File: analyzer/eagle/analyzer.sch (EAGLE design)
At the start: 32 parts, among them J4 USBSMD, U1 ATA6631, U2 FT232RL, U3 ATMEGA328P, U4 MOCD208M, X1 16MHz

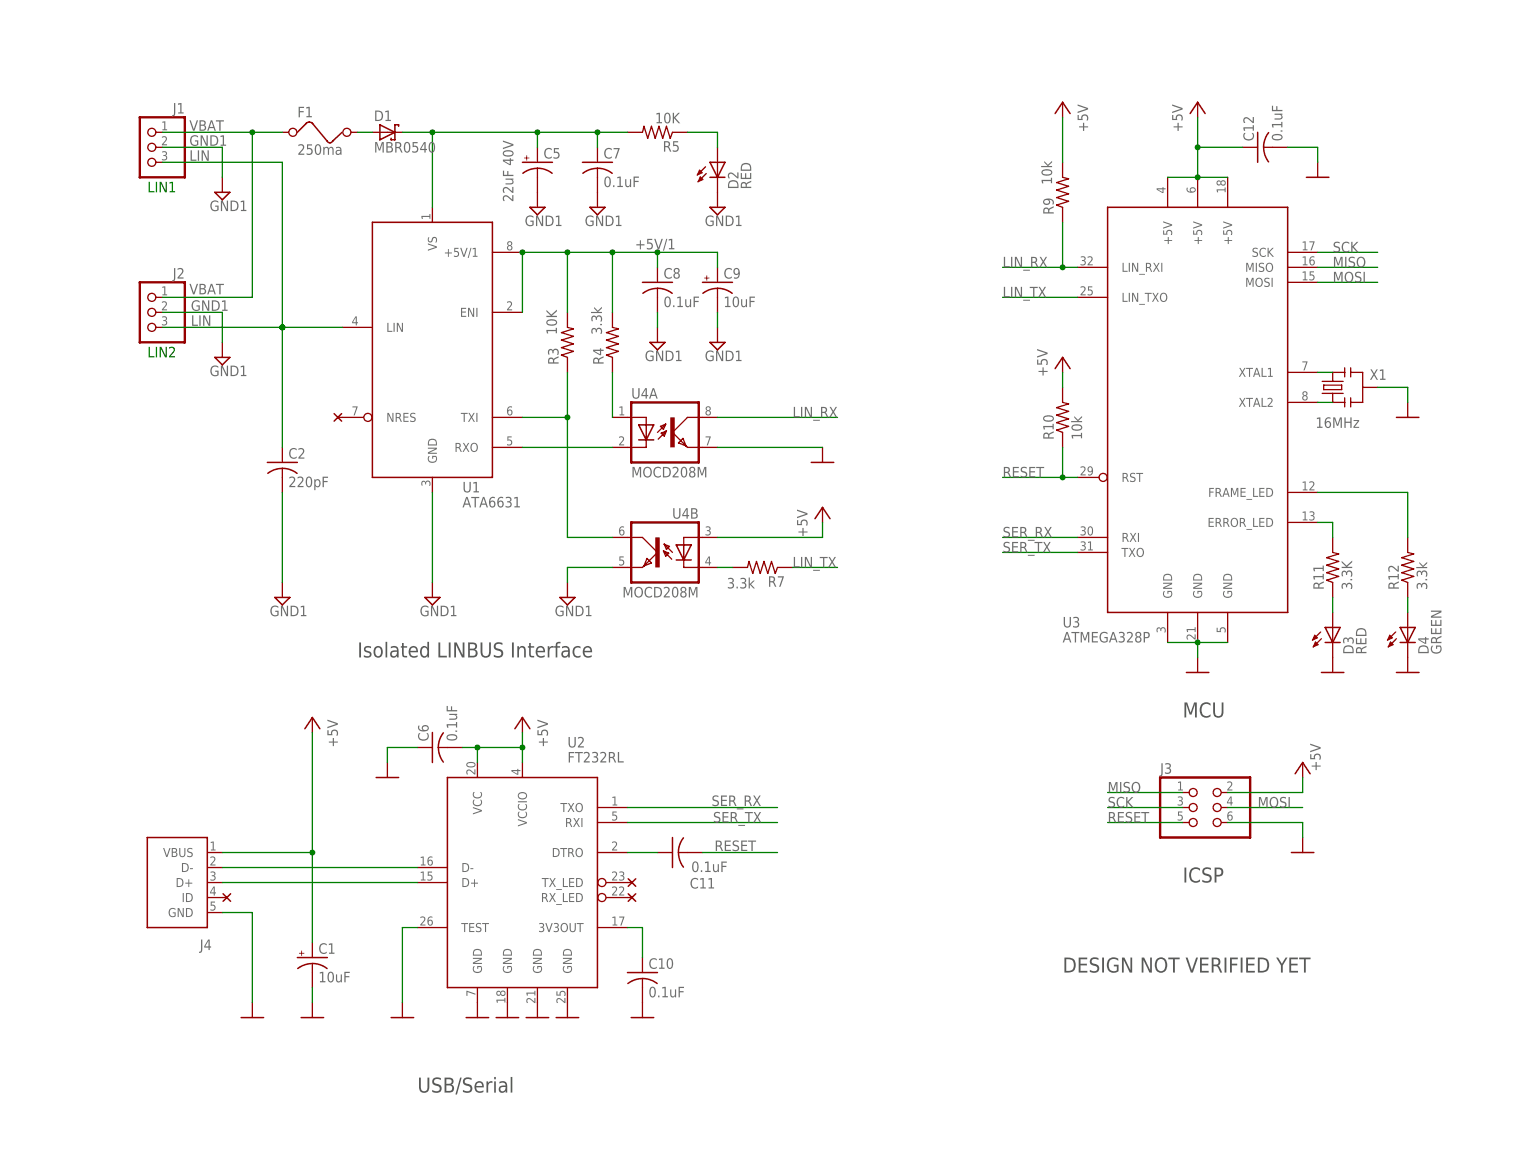
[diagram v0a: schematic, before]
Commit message: Manual Analyzer routing completed. Next will run auto router on signal nets.
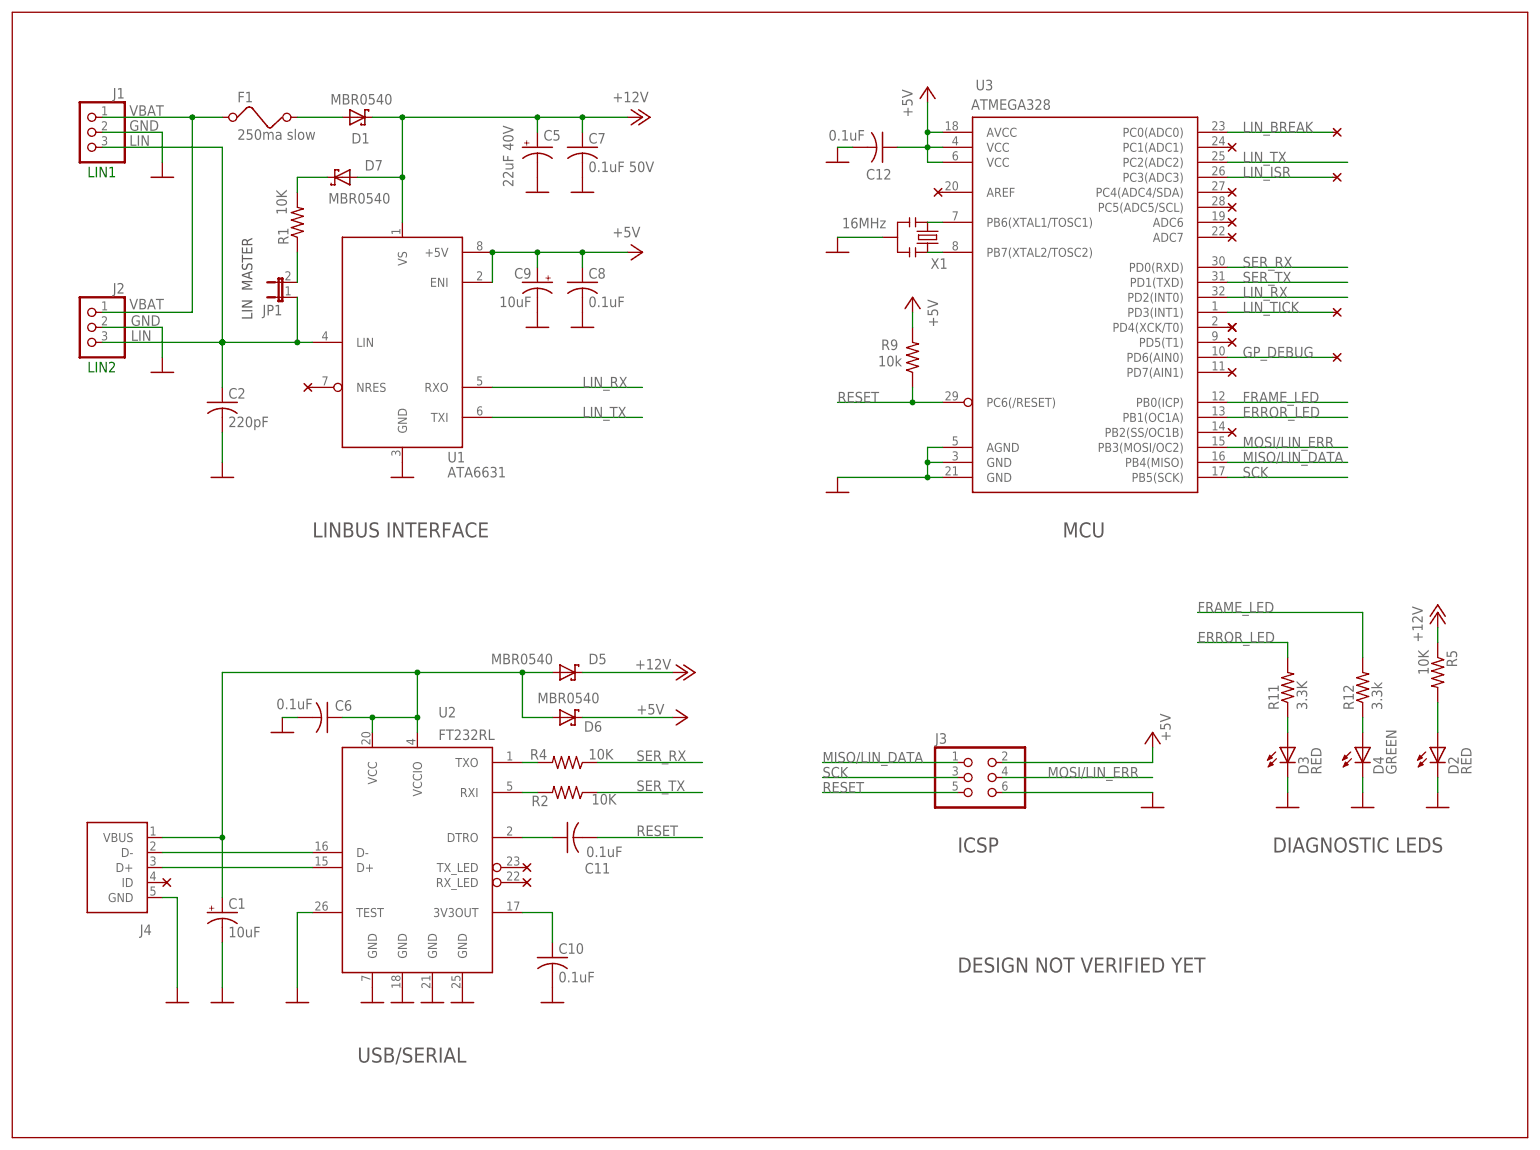
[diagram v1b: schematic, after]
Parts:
- removed R10: 10k, rcl:R-US_R0805
- removed R3: 10K, rcl:R-US_R0805
- removed R7: 3.3k, rcl:R-US_R0805
- removed U4: MOCD208M, optocoupler:MOCD208M
- added D5, D6, D7: MBR0540, analyzer:SMF5.0AT1
- added JP1: (no value), jumper:JP1E
- added R1, R2: 10K, analyzer:R-US_R0805
- C1, C9: device rcl:CPOL-USA/3216-18R -> analyzer:CPOL-USA/3216-18R
- C10, C11, C12, C2, C6, C8: device rcl:C-USC0805 -> analyzer:C-USC0805
- C5: device rcl:CPOL-USUD-6,3X5,8 -> analyzer:CPOL-USUD-6,3X5,8
- C7: value 0.1uF -> 0.1uF 50V; device rcl:C-USC0805 -> analyzer:C-USC0805
- D1: device diode:SMF5.0AT1 -> analyzer:SMF5.0AT1
- D2, D3, D4: device led:LEDSMT1206 -> analyzer:LED
- F1: value 250ma -> 250ma slow
- J1, J2: device pinhead:PINHD-1X3 -> analyzer:PINHD-1X3
- J3: device pinhead:PINHD-2X3 -> analyzer:PINHD-2X3
- R11, R12, R5, R9: device rcl:R-US_R0805 -> analyzer:R-US_R0805
- R4: value 3.3k -> 10K; device rcl:R-US_R0805 -> analyzer:R-US_R0805
- U3: value ATMEGA328P -> ATMEGA328; device analyzer:ATMEGA328P -> analyzer:ATMEGA328
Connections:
- removed net +5V/1: C8.1, C9.+, R3.2, R4.2, U1.+5V/1, U1.ENI
- removed net GND1: C2.2, C5.-, C7.2, C8.2, C9.-, D2.C, J1.2, J2.2, U1.GND, U4B.EMIT
- removed net MISO: J3.1, U3.MISO
- removed net MOSI: J3.4, U3.MOSI
- removed net N$1: R4.1, U4A.A
- removed net N$14: U3.XTAL2, X1.1
- new net ERROR_LED: R11.2, U3.PB1(OC1A)
- new net FRAME_LED: R12.2, U3.PB0(ICP)
- new net GP_DEBUG: U3.PD6(AIN0)
- new net LIN_BREAK: U3.PC0(ADC0)
- new net LIN_ISR: U3.PC3(ADC3)
- new net LIN_TICK: U3.PD3(INT1)
- new net MISO/LIN_DATA: J3.1, U3.PB4(MISO)
- new net MOSI/LIN_ERR: J3.4, U3.PB3(MOSI/OC2)
- new net N$2: U3.PB7(XTAL2/TOSC2), X1.1
- net +12V: now also D5.C, D7.A, R5.1; no longer R5.2
- net +5V: now also C8.1, C9.+, D6.C, U1.+5V, U1.ENI, U3.AVCC, U3.VCC@1, U3.VCC@2; no longer C1.+, C6.2, J4.VBUS, R10.2, U2.VCC, U2.VCCIO, U3.+5V@1, U3.+5V@2, U3.+5V@3, U4B.A
- net GND: now also C2.2, C5.-, C6.2, C7.2, C8.2, C9.-, D2.C, J1.2, J2.2, U1.GND, U3.AGND; no longer C6.1, U3.GND@3, U4A.EMIT
- net LIN: now also JP1.1
- net LIN_RX: now also U1.RXO, U3.PD2(INT0); no longer R9.1, U3.LIN_RXI, U4A.COL
- net LIN_TX: now also U1.TXI, U3.PC2(ADC2); no longer R7.1, U3.LIN_TXO
- net N$12: now also C1.+, C6.1, D5.A, D6.A, J4.VBUS, U2.VCC, U2.VCCIO; no longer R7.2, U4B.C
- net N$13: now also R4.2, U2.TXO; no longer U3.XTAL1, X1.3
- net N$17: now also R5.2; no longer R5.1
- net N$5: now also R2.2, U2.RXI; no longer U1.RXO, U4A.C
- net N$7: now also U3.PB6(XTAL1/TOSC1), X1.3; no longer R11.2, U3.ERROR_LED
- net N$8: now also D7.C, R1.2; no longer R12.2, U3.FRAME_LED
- net N$9: now also JP1.2, R1.1; no longer R3.1, U1.TXI, U4B.COL
- net RESET: now also R9.1, U3.PC6(/RESET); no longer R10.1, U3.RST
- net SCK: now also U3.PB5(SCK); no longer U3.SCK
- net SER_RX: now also R4.1, U3.PD0(RXD); no longer U2.TXO, U3.RXI
- net SER_TX: now also R2.1, U3.PD1(TXD); no longer U2.RXI, U3.TXO
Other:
- note added: "DIAGNOSTIC LEDS"
- note added: "LIN MASTER"
- note added: "LINBUS INTERFACE"
- note added: "USB/SERIAL"
- note removed: "Isolated LINBUS Interface"
- note removed: "USB/Serial"
- moved on the sheet: D1, D2, D3, D4, F1, J1, J2, J3, J4, R11, R12, R4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

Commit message: Completed the routing of the analyzer board.
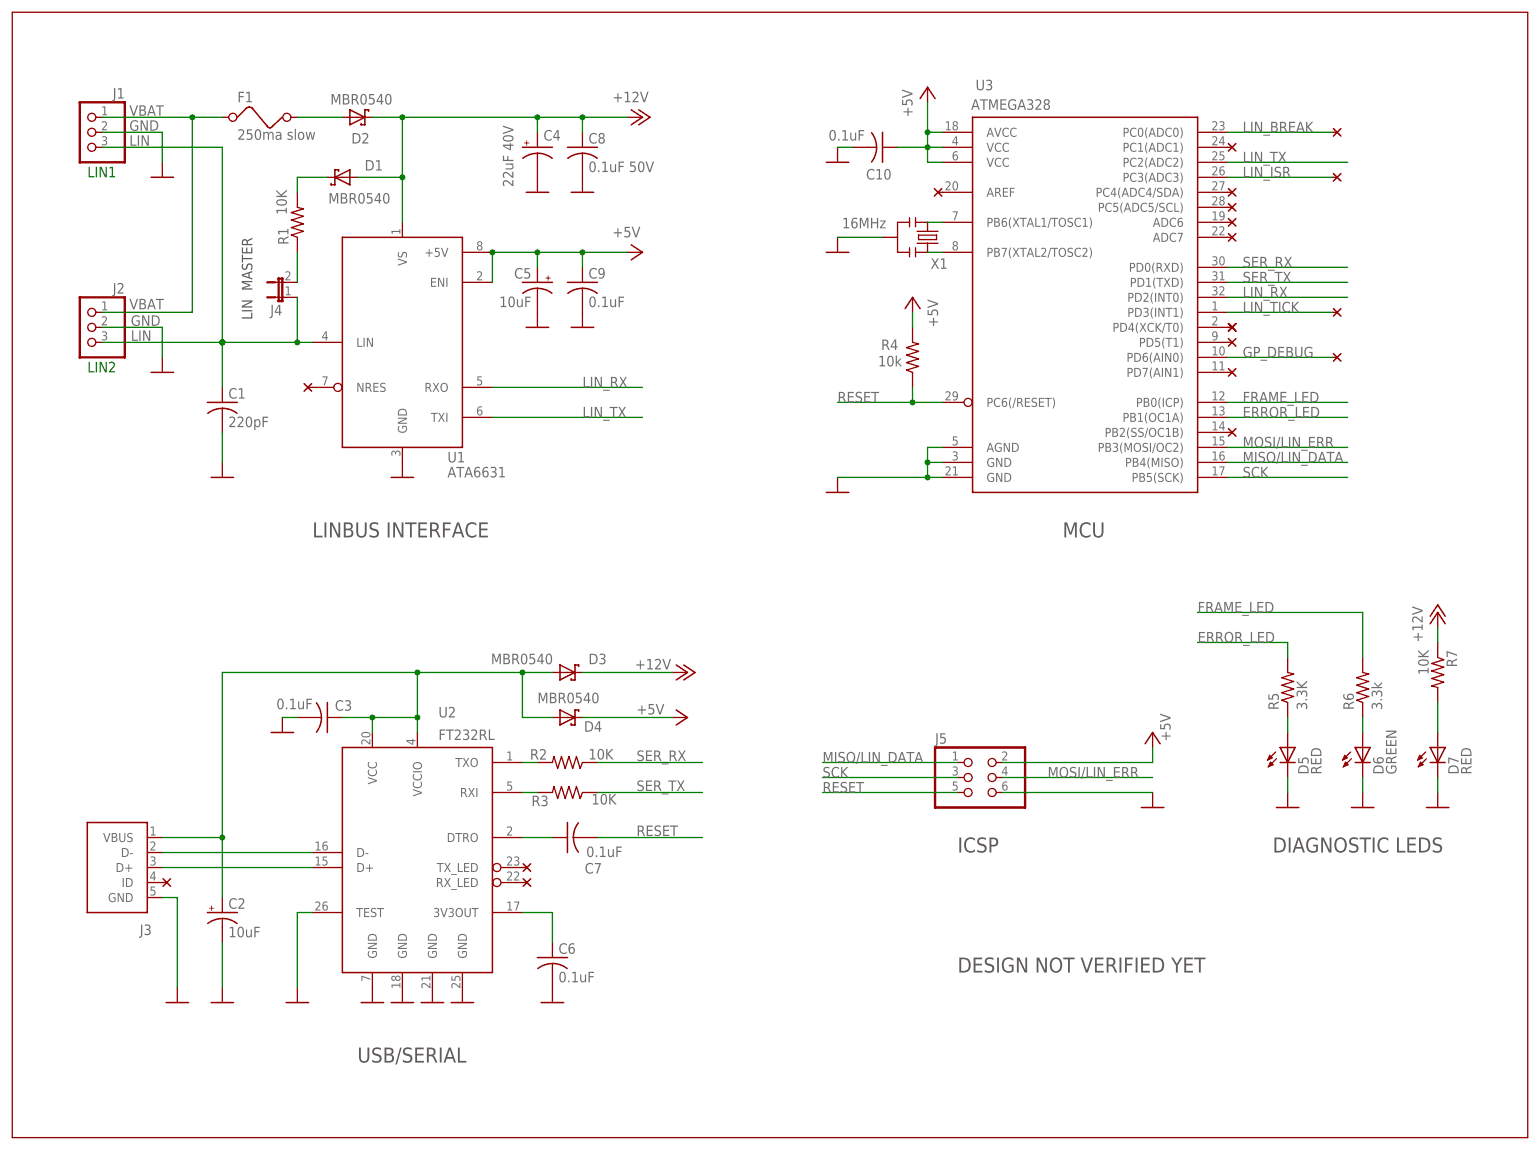
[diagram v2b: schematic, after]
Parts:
- removed C11, C12: 0.1uF, analyzer:C-USC0805
- removed JP1: (no value), jumper:JP1E
- removed R11: 3.3K, analyzer:R-US_R0805
- removed R9: 10k, analyzer:R-US_R0805
- added C3: 0.1uF, analyzer:C-USC0805
- added C4: 22uF 40V, analyzer:CPOL-USUD-6,3X5,8
- added J5: (no value), analyzer:PINHD-2X3
- added R3, R7: 10K, analyzer:R-US_R0805
- C1: value 10uF -> 220pF; device analyzer:CPOL-USA/3216-18R -> analyzer:C-USC0805
- C2: value 220pF -> 10uF; device analyzer:C-USC0805 -> analyzer:CPOL-USA/3216-18R
- C5: value 22uF 40V -> 10uF; device analyzer:CPOL-USUD-6,3X5,8 -> analyzer:CPOL-USA/3216-18R
- C7: value 0.1uF 50V -> 0.1uF
- C8: value 0.1uF -> 0.1uF 50V
- C9: value 10uF -> 0.1uF; device analyzer:CPOL-USA/3216-18R -> analyzer:C-USC0805
- D2, D3: value RED -> MBR0540; device analyzer:LED -> analyzer:SMF5.0AT1
- D4: value GREEN -> MBR0540; device analyzer:LED -> analyzer:SMF5.0AT1
- D5, D7: value MBR0540 -> RED; device analyzer:SMF5.0AT1 -> analyzer:LED
- D6: value MBR0540 -> GREEN; device analyzer:SMF5.0AT1 -> analyzer:LED
- J3: value (none) -> USBSMD; device analyzer:PINHD-2X3 -> analyzer:USBSMD
- J4: value USBSMD -> (none); device analyzer:USBSMD -> analyzer:JP1E
- R4: value 10K -> 10k
- R5: value 10K -> 3.3K
- renumbered R12 to R6
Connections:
- net +12V: now also C4.+, C8.1, D1.A, D2.C, D3.C, R7.1; no longer C5.+, C7.1, D1.C, D5.C, D7.A, R5.1
- net +5V: now also C10.1, C5.+, C9.1, D4.C, J5.2, R4.2; no longer C12.1, C8.1, C9.+, D6.C, J3.2, R9.2
- net ERROR_LED: now also R5.2; no longer R11.2
- net GND: now also C1.2, C2.-, C3.2, C4.-, C9.2, D5.C, D6.C, D7.C, J3.GND, J5.6; no longer C1.-, C12.2, C2.2, C7.2, C9.-, D2.C, D3.C, D4.C, J3.6, J4.GND
- net LIN: now also C1.1, J4.1; no longer C2.1, JP1.1
- net MISO/LIN_DATA: now also J5.1; no longer J3.1
- net MOSI/LIN_ERR: now also J5.4; no longer J3.4
- net N$10: now also J3.D+; no longer J4.D+
- net N$11: now also C7.1; no longer C11.1
- net N$12: now also C2.+, C3.1, D3.A, D4.A, J3.VBUS; no longer C1.+, C6.1, D5.A, D6.A, J4.VBUS
- net N$13: now also R2.2; no longer R4.2
- net N$15: now also J3.D-; no longer J4.D-
- net N$16: now also C6.1; no longer C10.1
- net N$17: now also D7.A, R7.2; no longer D2.A, R5.2
- net N$3: now also D6.A; no longer D4.A
- net N$4: now also D5.A, R5.1; no longer D3.A, R11.1
- net N$5: now also R3.2; no longer R2.2
- net N$6: now also D2.A; no longer D1.A
- net N$8: now also D1.C; no longer D7.C
- net N$9: now also J4.2; no longer JP1.2
- net RESET: now also C7.2, J5.5, R4.1; no longer C11.2, J3.5, R9.1
- net SCK: now also J5.3; no longer J3.3
- net SER_RX: now also R2.1; no longer R4.1
- net SER_TX: now also R3.1; no longer R2.1
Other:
- moved on the sheet: C10, C5, C6, C7, C8, D1, R2, R4, R5

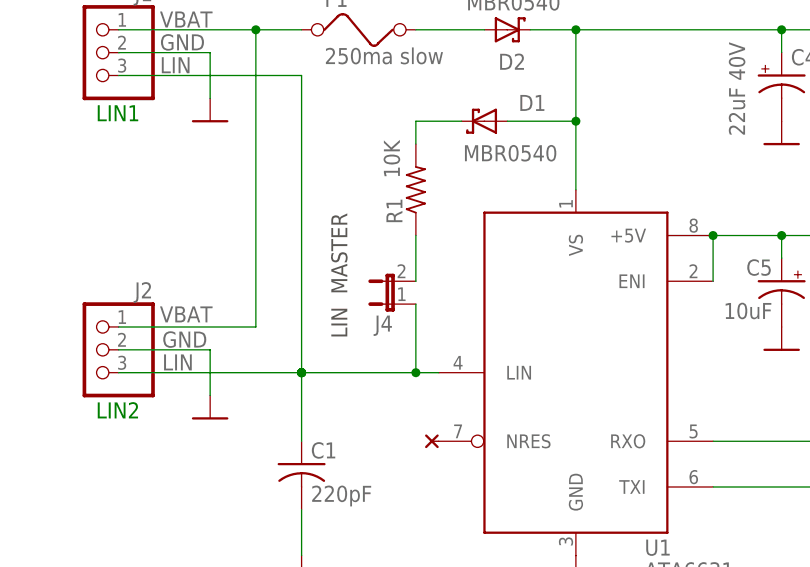
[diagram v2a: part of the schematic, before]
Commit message: Analyzer board layout completed.
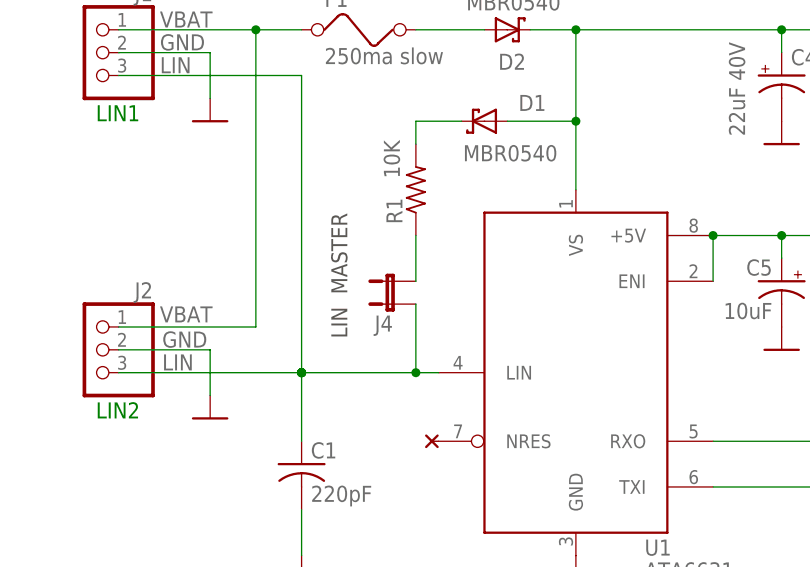
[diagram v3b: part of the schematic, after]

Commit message: Added analyzer flash image.
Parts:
- R1: value 10K -> 1K
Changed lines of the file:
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@@
 <part name="P+6" library="supply1" deviceset="+12V" device=""/>
 <part name="D1" library="analyzer" deviceset="SMF5.0AT1" device="" value="MBR0540"/>
-<part name="R1" library="analyzer" deviceset="R-US_" device="R0805" value="10K"/>
+<part name="R1" library="analyzer" deviceset="R-US_" device="R0805" value="1K"/>
 <part name="J4" library="analyzer" deviceset="JP1E" device=""/>
 <part name="P+8" library="supply1" deviceset="+12V" device=""/>
